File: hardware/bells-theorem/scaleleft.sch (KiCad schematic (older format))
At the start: 27 parts, among them U20 TL074, U21 TL072

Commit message: take gerbers out of the repo, push latest updates
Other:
- moved on the sheet: R116, R117
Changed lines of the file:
@@
 $Descr A4 11693 8268
 encoding utf-8
-Sheet 8 8
+Sheet 7 8
 Title ""
 Date ""
@@
 L device:R_Small_US R?
 U 1 1 5F89D22B
-P 2750 1900
+P 2750 1650
 AR Path="/5CEF66AD/5F9DE87B/5F89D22B" Ref="R?"  Part="1"
 AR Path="/5CEF66AD/5F8909DB/5F89D22B" Ref="R116"  Part="1"
-F 0 "R116" V 2545 1900 50  0000 C CNN
-F 1 "30K" V 2636 1900 50  0000 C CNN
-F 2 "Resistor_SMD:R_0805_2012Metric_Pad1.15x1.40mm_HandSolder" H 2750 1900 50  0001 C CNN
-F 3 "~" H 2750 1900 50  0001 C CNN
-	1    2750 1900
+F 0 "R116" V 2545 1650 50  0000 C CNN
+F 1 "30K" V 2636 1650 50  0000 C CNN
+F 2 "Resistor_SMD:R_0805_2012Metric_Pad1.15x1.40mm_HandSolder" H 2750 1650 50  0001 C CNN
+F 3 "~" H 2750 1650 50  0001 C CNN
+	1    2750 1650
 	0    1    1    0
 $EndComp
@@
 L device:R_Small_US R?
 U 1 1 5F89D231
-P 2750 2000
+P 2750 2150
 AR Path="/5CEF66AD/5F9DE87B/5F89D231" Ref="R?"  Part="1"
 AR Path="/5CEF66AD/5F8909DB/5F89D231" Ref="R117"  Part="1"
-F 0 "R117" V 2950 2000 50  0000 C CNN
-F 1 "30K" V 2850 2000 50  0000 C CNN
-F 2 "Resistor_SMD:R_0805_2012Metric_Pad1.15x1.40mm_HandSolder" H 2750 2000 50  0001 C CNN
-F 3 "~" H 2750 2000 50  0001 C CNN
-	1    2750 2000
+F 0 "R117" V 2950 2150 50  0000 C CNN
+F 1 "30K" V 2850 2150 50  0000 C CNN
+F 2 "Resistor_SMD:R_0805_2012Metric_Pad1.15x1.40mm_HandSolder" H 2750 2150 50  0001 C CNN
+F 3 "~" H 2750 2150 50  0001 C CNN
+	1    2750 2150
 	0    1    1    0
 $EndComp
@@
 $EndComp
 Wire Wire Line
-	2850 1900 3000 1900
-Wire Wire Line
-	3000 1900 3000 1650
+	2850 1650 3000 1650
 Wire Wire Line
 	3000 1650 3100 1650
@@
 	4100 1750 4150 1750
 Wire Wire Line
-	2850 2000 3000 2000
-Wire Wire Line
-	3000 2000 3000 2150
+	2850 2150 3000 2150
 Wire Wire Line
 	3000 2400 3100 2400
@@
 Connection ~ 6000 2600
 Wire Wire Line
-	2650 1900 2400 1900
-Wire Wire Line
-	2650 2000 2400 2000
+	2650 1650 2400 1650
+Wire Wire Line
+	2650 2150 2400 2150
 $Comp
 L power:+3.3V #PWR0218
@@
 	1    0    0    -1
 $EndComp
-Text HLabel 2400 2000 0    50   Input ~ 0
+Text HLabel 2400 2150 0    50   Input ~ 0
 CVA_in
-Text HLabel 2400 1900 0    50   Input ~ 0
+Text HLabel 2400 1650 0    50   Input ~ 0
 CVB_in
 Text HLabel 2400 3850 0    50   Input ~ 0

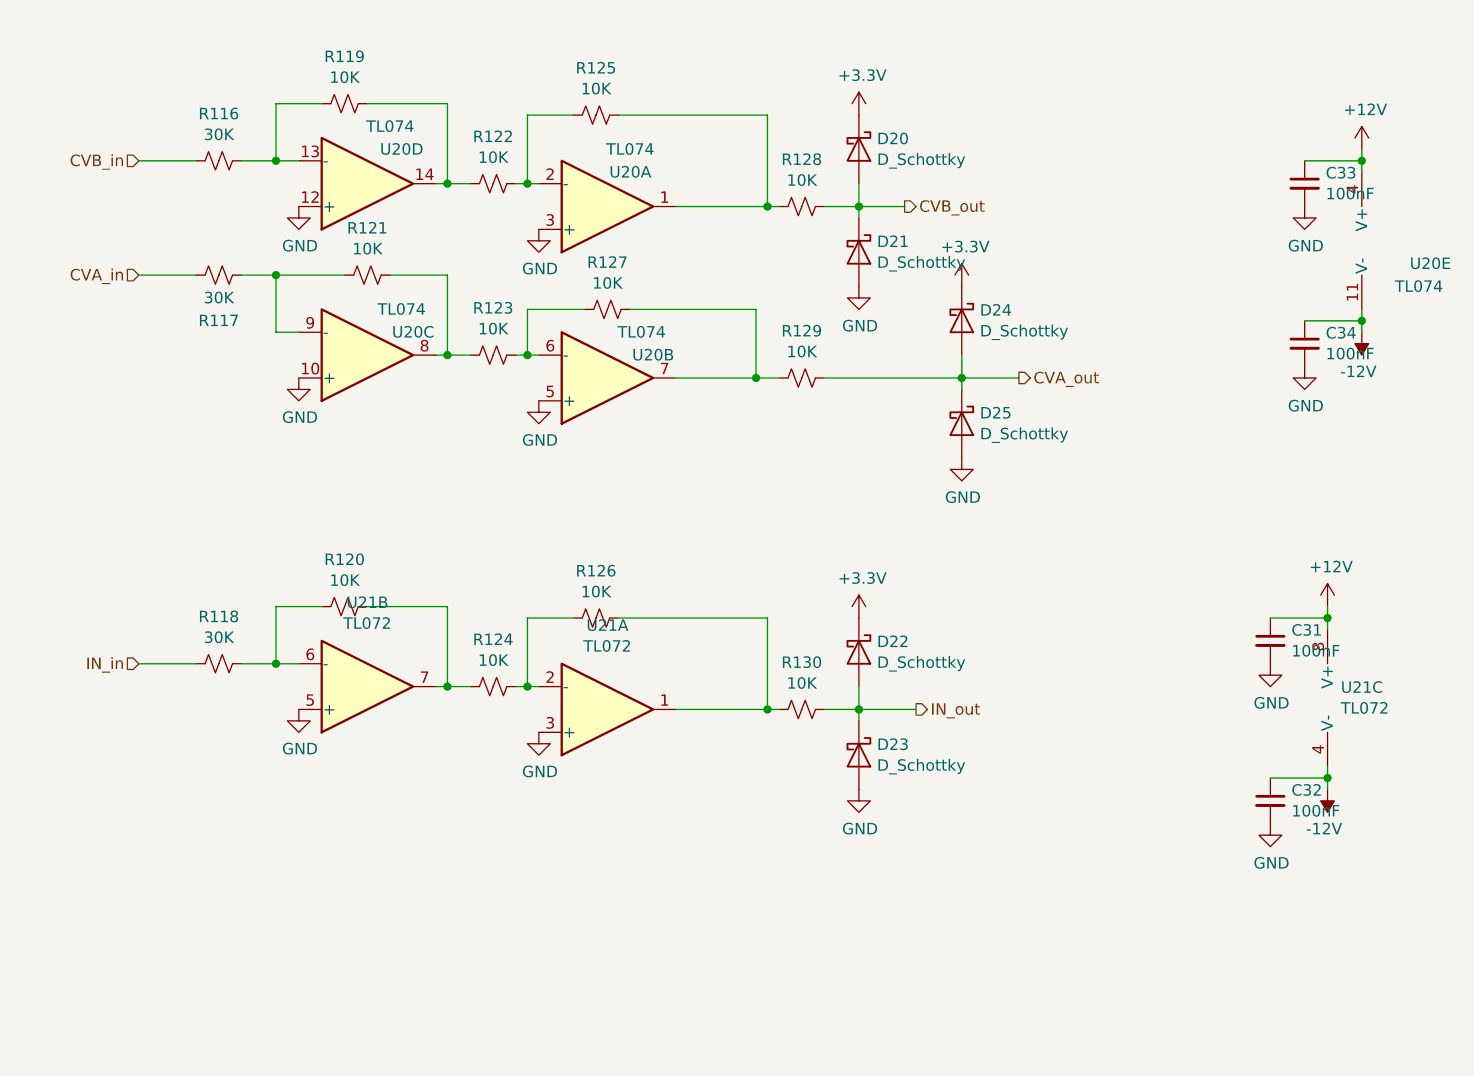
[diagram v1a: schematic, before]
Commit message: modified for Kicad 6 updated testing code
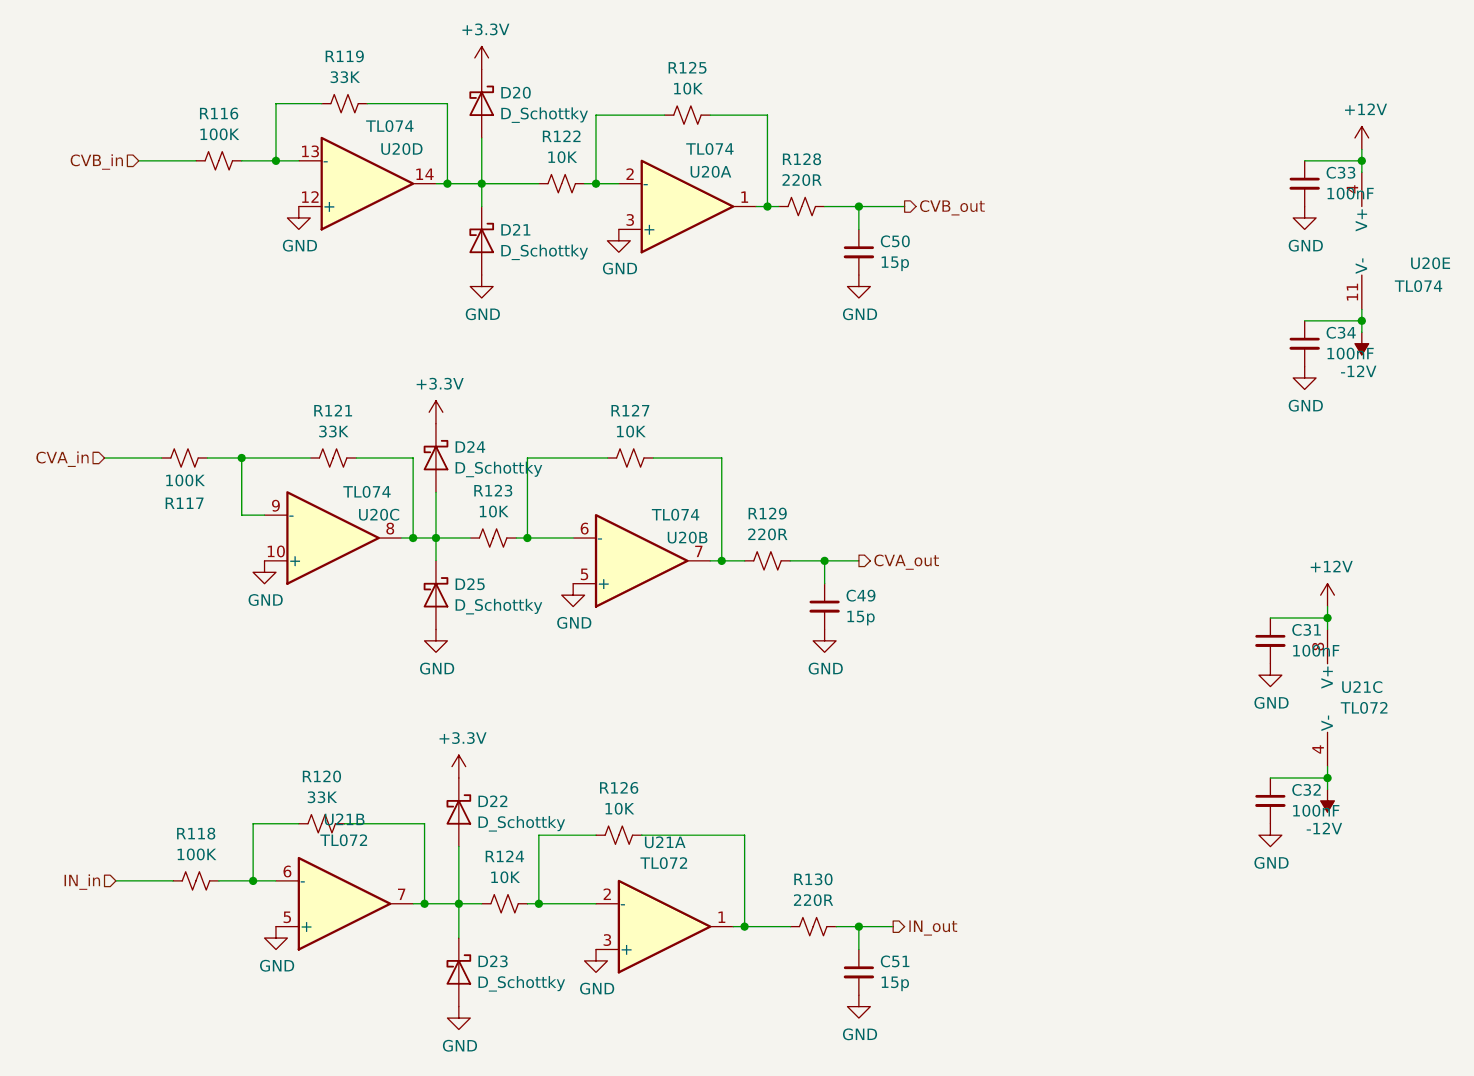
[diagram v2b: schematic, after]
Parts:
- added C49, C50, C51: 15p, symbol device:C_Small
- R116, R117, R118: value 30K -> 100K
- R119, R120, R121: value 10K -> 33K
- R128, R129, R130: value 10K -> 220R
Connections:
- net CVA_out: now also C49.1; no longer D24.2 (A), D25.1 (K)
- net CVB_out: now also C50.1; no longer D20.2 (A), D21.1 (K)
- net GND: now also C49.2, C50.2, C51.2
- net IN_out: now also C51.1; no longer D22.2 (A), D23.1 (K)
- net at R119.1, R122.2, U20.14: now also D20.2 (A), D21.1 (K)
- net at R121.1, R123.2, U20.8: now also D24.2 (A), D25.1 (K)
- net at R120.1, R124.2, U21.7: now also D22.2 (A), D23.1 (K)
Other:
- moved on the sheet: D20, D21, D22, D23, D24, D25, R117, R118, R120, R121, R122, R123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
